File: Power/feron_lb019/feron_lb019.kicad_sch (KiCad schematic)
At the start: 51 parts, among them J1 Conn_4pin01, J2 Conn_3pin01, P1 PC817, T1 TF8N60, U2 TL431, U3 OB2268

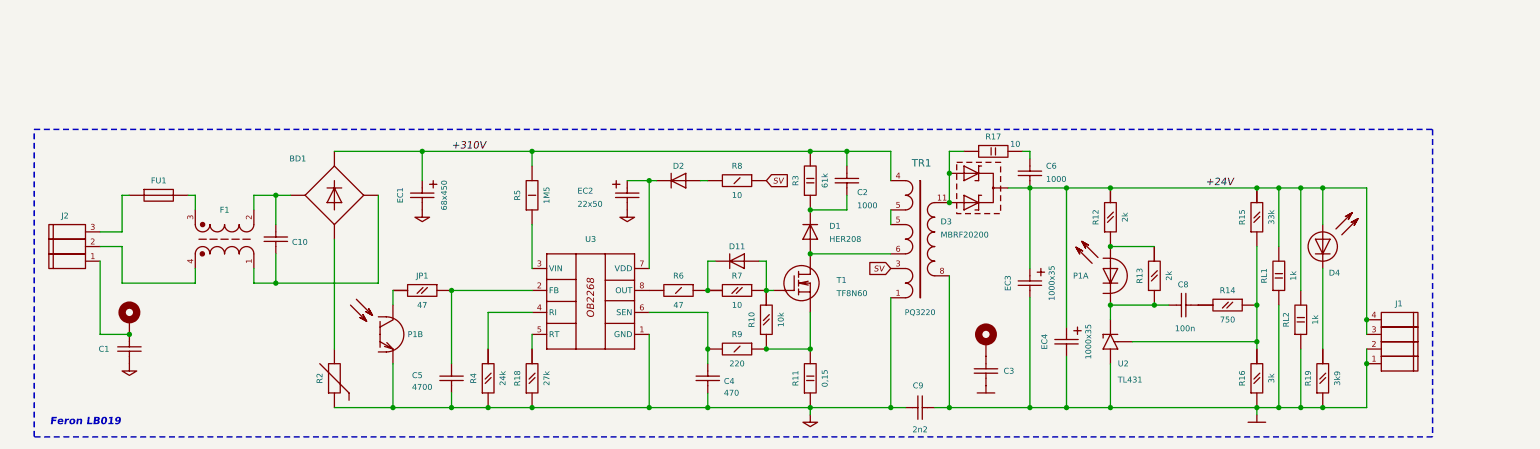
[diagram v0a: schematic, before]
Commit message: R6. +24V, R1
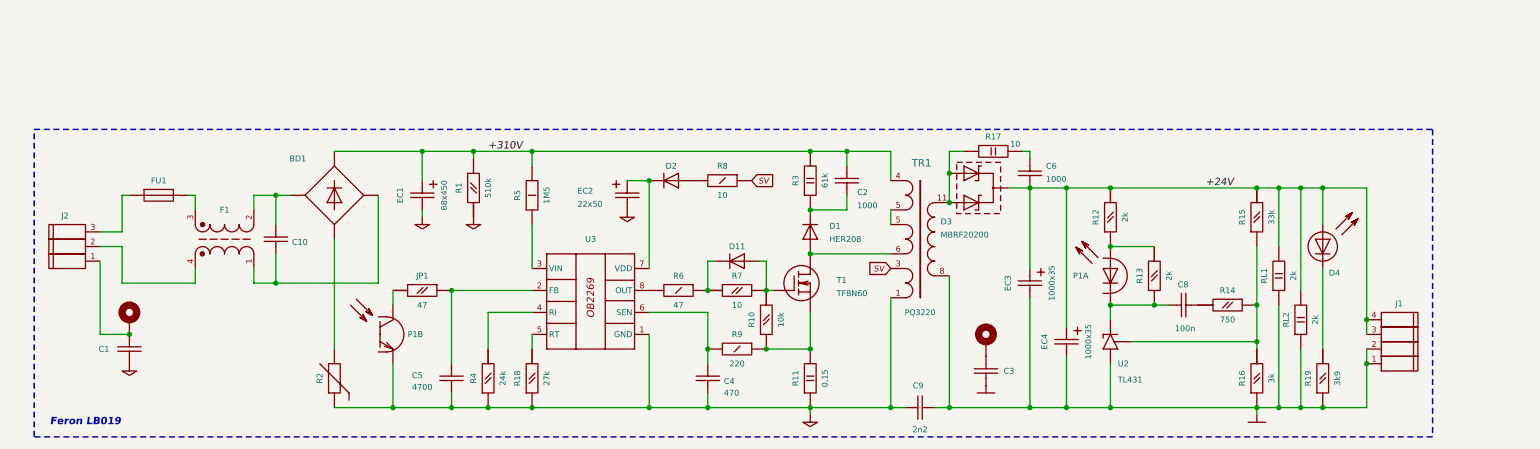
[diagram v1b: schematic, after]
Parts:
- added R1: 510k, Resistor_THT:R_Axial_DIN0207_L6.3mm_D2.5mm_P10.16mm_Horizontal, symbol _aa40_resistors:R_RES_0.125W
- RL1, RL2: value 1k -> 2k
- U3: symbol _aa40_chips:OB2268 -> _aa40_chips:OB2269
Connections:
- net +310V: now also R1.1
- net GND1: now also R1.2
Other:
- moved on the sheet: D2, R8
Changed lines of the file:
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@@
 	)
 	(junction
+		(at 97.79 43.18)
+		(diameter 0)
+		(color 0 0 0 0)
+	)
+	(junction
 		(at 156.21 77.47)
 		(diameter 0)
@@
 	(wire
 		(pts
-			(xy 138.43 48.26) (xy 137.16 48.26)
+			(xy 97.79 43.18) (xy 107.95 43.18)
 		)
 		(stroke
@@
 	(wire
 		(pts
-			(xy 88.9 43.18) (xy 107.95 43.18)
+			(xy 88.9 43.18) (xy 97.79 43.18)
 		)
 		(stroke
@@
 	(wire
 		(pts
-			(xy 170.18 43.18) (xy 170.18 48.26)
+			(xy 97.79 43.18) (xy 97.79 44.45)
 		)
 		(stroke
@@
 	(wire
 		(pts
-			(xy 129.54 48.26) (xy 128.27 48.26)
+			(xy 170.18 43.18) (xy 170.18 48.26)
 		)
 		(stroke
@@
 	(wire
 		(pts
+			(xy 88.9 54.61) (xy 88.9 53.34)
+		)
+		(stroke
+			(width 0)
+			(type default)
+		)
+	)
+	(wire
+		(pts
 			(xy 194.31 49.53) (xy 194.31 63.5)
 		)
@@
 	)
 	(label "+310V"
-		(at 93.98 43.18 0)
+		(at 100.33 43.18 0)
 		(fields_autoplaced yes)
 		(effects
@@
 	(global_label "SV"
 		(shape input)
-		(at 148.59 48.26 0)
+		(at 146.05 48.26 0)
 		(fields_autoplaced yes)
 		(effects
@@
 		)
 		(property "Intersheetrefs" "${INTERSHEET_REFS}"
-			(at 152.8164 48.26 0)
+			(at 150.2764 48.26 0)
 			(effects
 				(font
@@
 	)
 	(symbol
+		(lib_id "_aa40_misc:GND1")
+		(at 97.79 54.61 0)
+		(unit 1)
+		(exclude_from_sim no)
+		(in_bom yes)
+		(on_board yes)
+		(dnp no)
+		(fields_autoplaced yes)
+		(property "Reference" "#PWR01"
+			(at 97.79 60.96 0)
+			(effects
+				(font
+					(size 1.27 1.27)
+				)
+				(hide yes)
+			)
+		)
+		(property "Value" "GND1"
+			(at 97.79 58.42 0)
+			(effects
+				(font
+					(size 1.27 1.27)
+				)
+				(hide yes)
+			)
+		)
+		(property "Footprint" ""
+			(at 97.79 54.61 0)
+			(effects
+				(font
+					(size 1.27 1.27)
+				)
+				(hide yes)
+			)
+		)
+		(property "Datasheet" ""
+			(at 97.79 54.61 0)
+			(effects
+				(font
+					(size 1.27 1.27)
+				)
+				(hide yes)
+			)
+		)
+		(property "Description" "Power symbol creates a global label with name \"GND1\" , ground"
+			(at 97.79 54.61 0)
+			(effects
+				(font
+					(size 1.27 1.27)
+				)
+				(hide yes)
+			)
+		)
+		(pin "1"
+		)
+		(instances
+			(project "feron_lb019"
+				(path "/2231a296-fb6b-43a8-92d6-581e2d66b47b"
+					(reference "#PWR01")
+					(unit 1)
+				)
+			)
+		)
+	)
+	(symbol
 		(lib_id "_aa40_capacitors:C_CAP")
 		(at 93.98 82.55 90)
@@
 			)
 		)
-		(property "Value" "1k"
+		(property "Value" "2k"
 			(at 240.03 64.77 0)
 			(effects
@@
 	(symbol
 		(lib_id "_aa40_resistors:R_RES_0.25")
-		(at 143.51 48.26 0)
+		(at 140.97 48.26 0)
 		(mirror y)
 		(unit 1)
@@
 		(dnp no)
 		(property "Reference" "R8"
-			(at 143.51 45.72 0)
+			(at 140.97 45.72 0)
 			(effects
 				(font
@@
 		)
 		(property "Value" "10"
-			(at 143.51 50.8 0)
+			(at 140.97 50.8 0)
 			(effects
 				(font
@@
 		)
 		(property "Footprint" "Resistor_THT:R_Axial_DIN0207_L6.3mm_D2.5mm_P10.16mm_Horizontal"
-			(at 143.51 48.26 0)
+			(at 140.97 48.26 0)
 			(effects
 				(font
@@
 		)
 		(property "Datasheet" ""
-			(at 143.51 48.26 0)
+			(at 140.97 48.26 0)
 			(effects
 				(font
@@
 		)
 		(property "Description" "Резистор 0,25 Ватт"
-			(at 143.51 48.26 0)
+			(at 140.97 48.26 0)
 			(effects
 				(font
@@
 	(symbol
 		(lib_id "_aa40_misc:GND1")
-		(at 88.9 53.34 0)
+		(at 88.9 54.61 0)
 		(unit 1)
 		(exclude_from_sim no)
@@
 		(fields_autoplaced yes)
 		(property "Reference" "#PWR08"
-			(at 88.9 59.69 0)
+			(at 88.9 60.96 0)
 			(effects
 				(font
@@
 		)
 		(property "Value" "GND1"
-			(at 88.9 57.15 0)
+			(at 88.9 58.42 0)
 			(effects
 				(font
@@
 		)
 		(property "Footprint" ""
-			(at 88.9 53.34 0)
+			(at 88.9 54.61 0)
 			(effects
 				(font
@@
 		)
 		(property "Datasheet" ""
-			(at 88.9 53.34 0)
+			(at 88.9 54.61 0)
 			(effects
 				(font
@@
 		)
 		(property "Description" "Power symbol creates a global label with name \"GND1\" , ground"
-			(at 88.9 53.34 0)
+			(at 88.9 54.61 0)
 			(effects
 				(font
@@
 	)
 	(symbol
-		(lib_id "_aa40_chips:OB2268")
+		(lib_id "_aa40_chips:OB2269")
 		(at 118.11 68.58 0)
 		(unit 1)
@@
 	(symbol
 		(lib_id "_aa40_diodes:DIODE")
-		(at 133.35 48.26 0)
+		(at 132.08 48.26 0)
 		(mirror y)
 		(unit 1)
@@
 		(dnp no)
 		(property "Reference" "D2"
-			(at 133.35 45.72 0)
+			(at 132.08 45.72 0)
 			(effects
 				(font
@@
 		)
 		(property "Value" "DIODE"
-			(at 133.35 50.8 0)
+			(at 132.08 50.8 0)
 			(effects
 				(font
@@
 		)
 		(property "Footprint" "Diode_THT:D_A-405_P10.16mm_Horizontal"
-			(at 133.35 60.96 0)
+			(at 132.08 60.96 0)
 			(effects
 				(font
@@
 		)
 		(property "Datasheet" ""
-			(at 133.35 60.96 0)
+			(at 132.08 60.96 0)
 			(effects
 				(font
@@
 		)
 		(property "Description" "Диод"
-			(at 133.35 48.26 0)
+			(at 132.08 48.26 0)
 			(effects
 				(font
@@
 	)
 	(symbol
+		(lib_id "_aa40_resistors:R_RES_0.125W")
+		(at 97.79 49.53 90)
+		(mirror x)
+		(unit 1)
+		(exclude_from_sim no)
+		(in_bom yes)
+		(on_board yes)
+		(dnp no)
+		(property "Reference" "R1"
+			(at 95.25 49.53 0)
+			(effects
+				(font
+					(size 1.016 1.016)
+				)
+			)
+		)
+		(property "Value" "510k"
+			(at 100.33 49.53 0)
+			(effects
+				(font
+					(size 1.016 1.016)
+				)
+			)
+		)
+		(property "Footprint" "Resistor_THT:R_Axial_DIN0207_L6.3mm_D2.5mm_P10.16mm_Horizontal"
+			(at 100.33 45.72 0)
+			(effects
+				(font
+					(size 1.778 1.778)
+				)
+				(hide yes)
+			)
+		)
+		(property "Datasheet" ""
+			(at 97.79 49.53 0)
+			(effects
+				(font
+					(size 1.778 1.778)
+				)
+				(hide yes)
+			)
+		)
+		(property "Description" "Резистор 0.125 Ватт"
+			(at 97.79 49.53 0)
+			(effects
+				(font
+					(size 1.27 1.27)
+				)
+				(hide yes)
+			)
+		)
+		(pin "1"
+		)
+		(pin "2"
+		)
+		(instances
+			(project "feron_lb019"
+				(path "/2231a296-fb6b-43a8-92d6-581e2d66b47b"
+					(reference "R1")
+					(unit 1)
+				)
+			)
+		)
+	)
+	(symbol
 		(lib_id "_aa40_capacitors:C_CAP")
 		(at 220.98 69.85 180)
@@
 			)
 		)
-		(property "Value" "1k"
+		(property "Value" "2k"
 			(at 243.84 72.39 0)
 			(effects

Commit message: R15R16
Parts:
- R15: value 33k -> 27k
- R16: value 3k -> 3k3
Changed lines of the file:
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@@
 			)
 		)
-		(property "Value" "33k"
+		(property "Value" "27k"
 			(at 236.22 54.61 0)
 			(effects
@@
 			)
 		)
-		(property "Value" "3k"
+		(property "Value" "3k3"
 			(at 236.22 82.55 0)
 			(effects

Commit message: Add L1R20C7
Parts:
- removed RL2: 2k, Resistor_THT:R_Axial_DIN0516_L15.5mm_D5.0mm_P20.32mm_Horizontal, symbol _aa40_resistors:R_RES_2.0W
- added C7: NA, Capacitor_THT:C_Disc_D5.0mm_W2.5mm_P5.00mm, symbol _aa40_capacitors:C_CAP
- added EC5: 1000x35, Capacitor_THT:CP_Radial_D10.0mm_P5.00mm, symbol _aa40_capacitors:C_CAP_PLUS
- added L1: LFERR, _aTransformers:dross03, symbol _aa40_inductors:LFERR
- added R20: NA, Resistor_THT:R_Axial_DIN0207_L6.3mm_D2.5mm_P10.16mm_Horizontal, symbol _aa40_resistors:R_RES_0.125W
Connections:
- net +24V: now also EC5.1, L1.2; no longer C6.1, D3.2 (K), EC3.1, EC4.1, RL1.2
- net GND: now also EC5.2
- net at C8.2, P1.2 (C), R13.1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: now also R20.2
- net at R14.1, R15.1, R16.2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: now also C7.1
- new net: C7.2, R20.1
- new net: C6.1, D3.2 (K), EC3.1, EC4.1, L1.1, RL1.2
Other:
- moved on the sheet: BD1, C1, C10, C2, C3, C4, C5, C6, C8, C9, D1, D11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

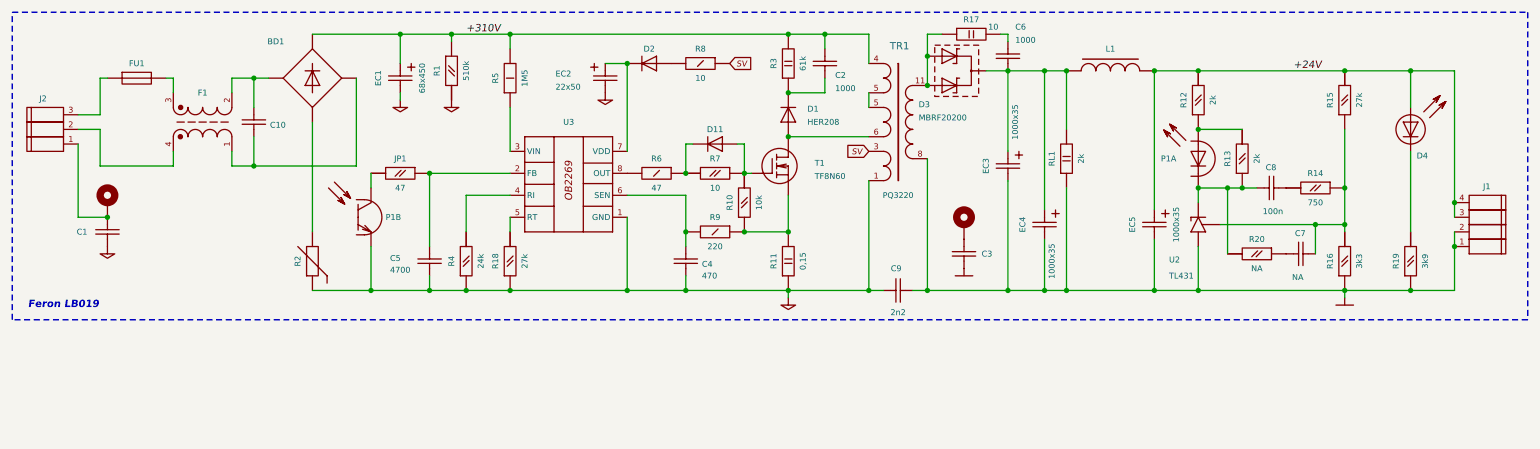
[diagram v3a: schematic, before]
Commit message: L1 betw R12&R15
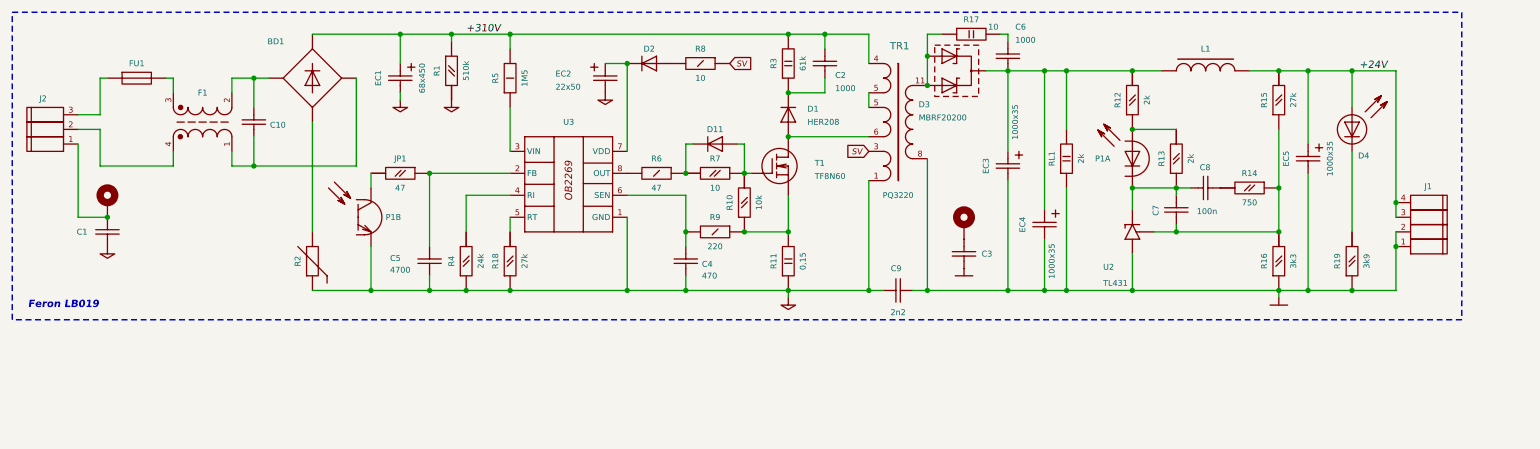
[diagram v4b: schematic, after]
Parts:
- removed R20: NA, Resistor_THT:R_Axial_DIN0207_L6.3mm_D2.5mm_P10.16mm_Horizontal, symbol _aa40_resistors:R_RES_0.125W
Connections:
- net +24V: no longer R12.2
- net at R14.1, R15.1, R16.2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: now also C7.2; no longer C7.1
- net at C8.2, P1.2 (C), R13.1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: now also C7.1
- net at C6.1, D3.2 (K), EC3.1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: now also R12.2
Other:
- moved on the sheet: C7, C8, D4, EC5, J1, L1, P1A, R12, R13, R14, R15, R16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

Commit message: R15R16
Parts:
- R15: value 27k -> 13k
- R16: value 3k3 -> 1k5
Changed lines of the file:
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@@
 			)
 		)
-		(property "Value" "27k"
+		(property "Value" "13k"
 			(at 240.03 34.29 0)
 			(effects
@@
 			)
 		)
-		(property "Value" "3k3"
+		(property "Value" "1k5"
 			(at 240.03 62.23 0)
 			(effects
